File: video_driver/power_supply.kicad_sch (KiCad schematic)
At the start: 14 parts, among them J1 USB_C_Receptacle_USB2.0_16P, J2 5.5OD_2.1ID, U3 ADP2105ACPZ-3.3-R7, U4 TPS7A20xxxDBV, U5 TPS7A20xxxDBV

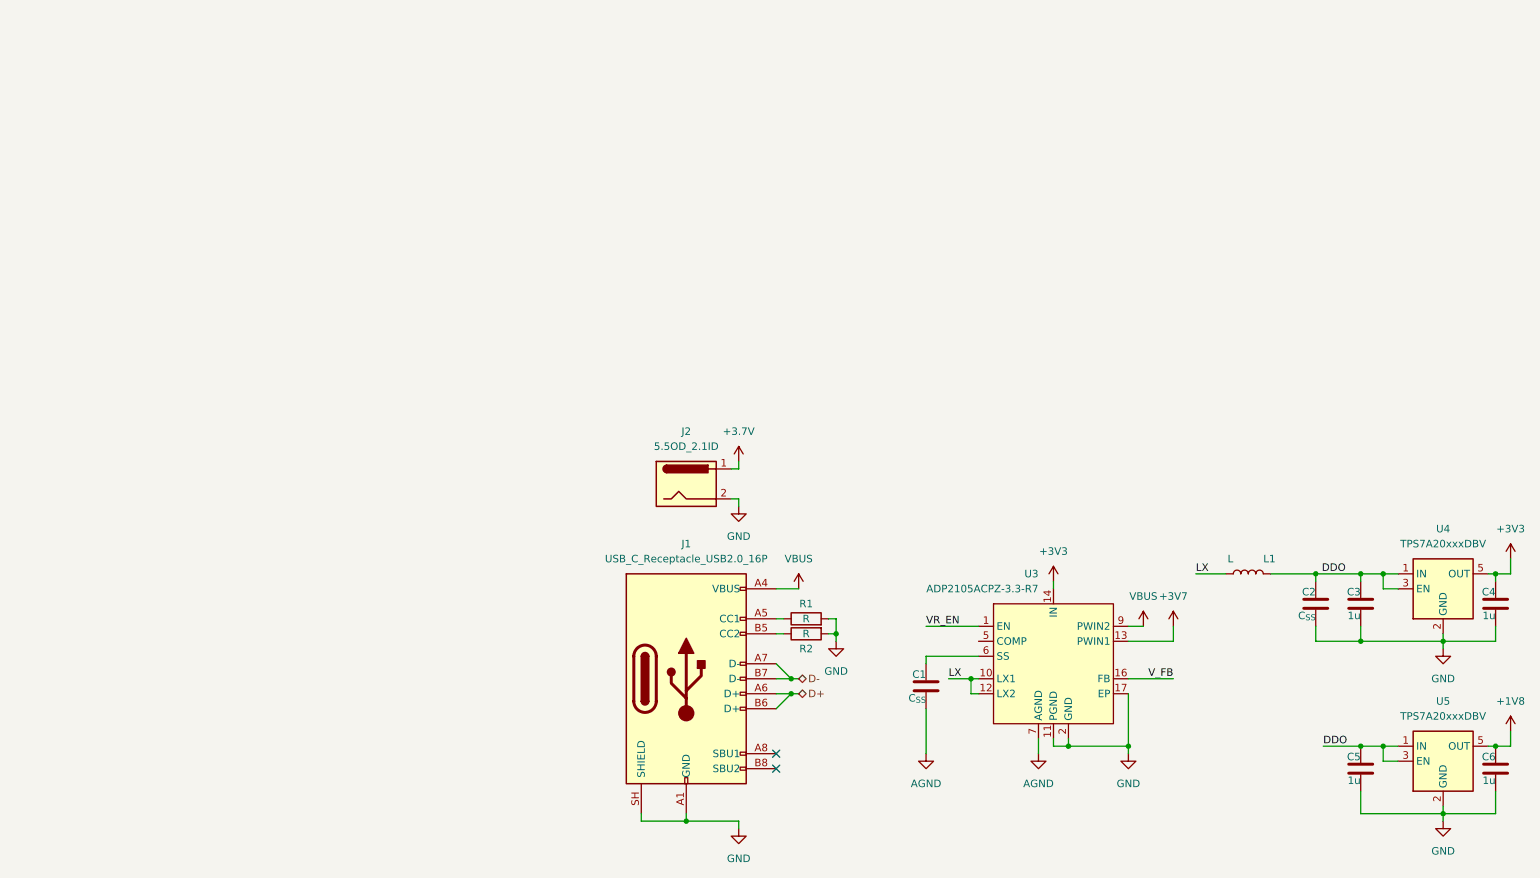
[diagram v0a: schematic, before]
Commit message: power supply start
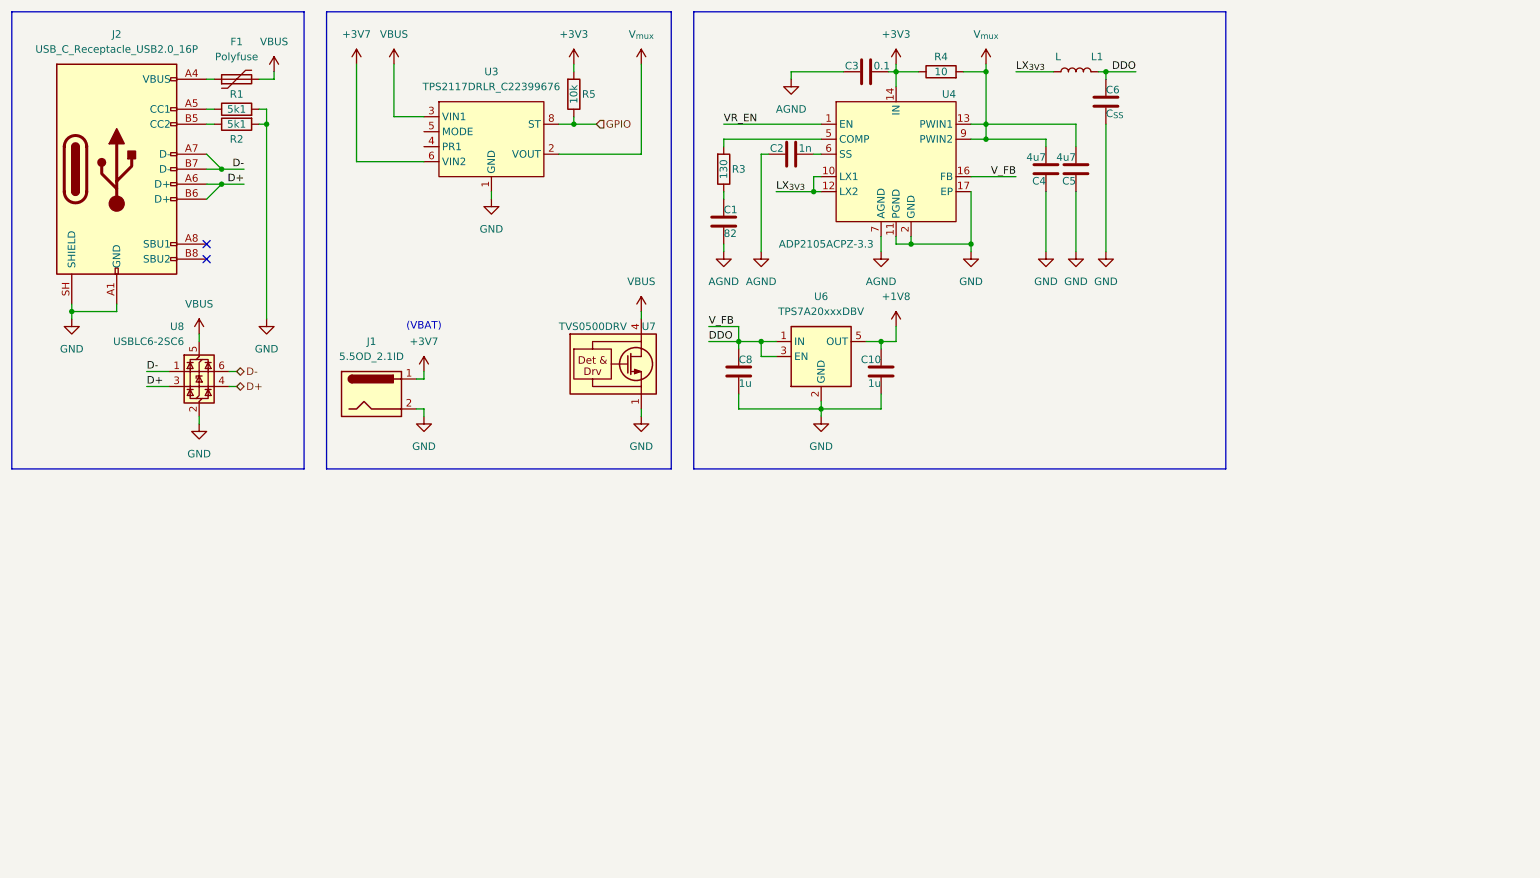
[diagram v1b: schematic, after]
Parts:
- removed U4: TPS7A20xxxDBV, Package_TO_SOT_SMD:SOT-23-5, symbol Regulator_Linear:TPS7A20xxxDBV
- added C1: 82, symbol Device:C
- added C5: 4u7, symbol Device:C
- added F1: Polyfuse, symbol Device:Polyfuse
- added R3: 130, symbol Device:R
- added R4: 10, symbol Device:R
- added R5: 10k, symbol Device:R
- added U3: TPS2117DRLR_C22399676, EasyEDA:SOT-583-8_L2.1-W1.2-P0.50-LS1.6-BL, symbol EasyEDA:TPS2117DRLR_C22399676
- added U7: TVS0500DRV, Package_SON:WSON-6-1EP_2x2mm_P0.65mm_EP1x1.6mm, symbol Power_Protection:TVS0500DRV
- added U8: USBLC6-2SC6, Package_TO_SOT_SMD:SOT-23-6, symbol Power_Protection:USBLC6-2SC6
- C2: renamed from C1; value C_{SS} -> 1n
- C3: value 1u -> 0.1
- C4: value 1u -> 4u7
- R1, R2: value R -> 5k1
- U4: renamed from U3; value ADP2105ACPZ-3.3-R7 -> ADP2105ACPZ-3.3
- renumbered C6 to C10, C2 to C6, C5 to C8, J2 to J1, J1 to J2, U5 to U6
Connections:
- net +3.7V is gone; now on net +3V7: J1.1
- net V_FB is gone; now on net DDO: U4.16 (FB)
- net +3V3: now also C3.2, R4.1, R5.2; no longer C4.1
- net +3V7: now also U3.6 (VIN2); no longer U4.13 (PWIN1)
- net AGND: now also C2.1, C3.1, C1.2; no longer C2.2
- net D+: now also U8.3 (I/O2), U8.4 (I/O2)
- net D-: now also U8.1 (I/O1), U8.6 (I/O1)
- net DDO: no longer C3.1
- net GND: now also C4.1, C5.1, U3.1 (GND), U7.1 (GND), U7.2 (GND), U7.3 (GND), U7.7 (GND), U8.2 (GND); no longer C3.2, C4.2
- net VBUS: now also F1.2, U3.3 (VIN1), U7.4 (IN), U7.5 (IN), U7.6 (IN), U8.5 (VBUS); no longer J2.A4 (VBUS), J2.A9 (VBUS), J2.B4 (VBUS), J2.B9 (VBUS), U4.9 (PWIN2)
- net at U4.5 (COMP): now also R3.2
- net at U4.6 (SS): now also C2.2; no longer C2.1
- net LX renamed LX_{3V3}
- new net: C1.1, R3.1
- new net: F1.1, J2.A4 (VBUS), J2.A9 (VBUS), J2.B4 (VBUS), J2.B9 (VBUS)
- new net GPIO: R5.1, U3.8 (ST)
- new net V_{mux}: C4.2, C5.2, R4.2, U3.2 (VOUT), U3.7 (VOUT), U4.13 (PWIN1), U4.9 (PWIN2)
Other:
- note added: "(VBAT)"
- moved on the sheet: C10, C2, C6, C8, J1, J2, L1, R1, R2, U4, U6

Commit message: power supply work
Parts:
- added C15, C16, C17, C18: 1u, symbol Device:C
- added C9: 4u7, symbol Device:C
- added F2: Polyfuse, symbol Device:Polyfuse
- added R3, R4: 5k1, symbol Device:R
- added U8, U9: TPS7A20xxxDBV, Package_TO_SOT_SMD:SOT-23-5, symbol Regulator_Linear:TPS7A20xxxDBV
- C8: renamed from C6; value C_{SS} -> 10u
- L1: value L -> 4u1
- U4: renamed from U3; value TPS2117DRLR_C22399676 -> TPS2117DRLR
- renumbered C8 to C2, C2 to C3, C3 to C4, C10 to C5, C4 to C6, C5 to C7, J2 to J1, J1 to J2, R3 to R6, R4 to R7, U8 to U3, U7 to U5, U4 to U7
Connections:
- net DDO: now also C15.1, C17.1, C9.1, U8.1 (IN), U8.3 (EN), U9.1 (IN), U9.3 (EN)
- net GND: now also C6.2, C7.2, C15.2, C16.2, C17.2, C18.2, C9.2, R4.1, U8.2 (GND), U9.2 (GND); no longer C6.1, C7.1
- net VBUS: now also U4.5 (MODE), R3.2
- net V_{mux}: now also C6.1, C7.1; no longer C6.2, C7.2
- net T_{switch}: now reaches U4.4 (PR1)
- net T_{switch}: now also R3.1, R4.2
- net +1V8 renamed +1V8_{P}
- net +3V7: no longer names the net of J2.1
- net +3V7: now also F2.2; no longer U4.6 (VIN2)
- new net +1V8_{A}: C16.1, U8.5 (OUT)
- new net +1V8_{D}: C18.1, U9.5 (OUT)
- new net VBAT: F2.1, U4.6 (VIN2)
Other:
- note added: "(+3V7)"
- note added: "V_{mux} OUT"
- note removed: "(VBAT)"
- moved on the sheet: C8, U3

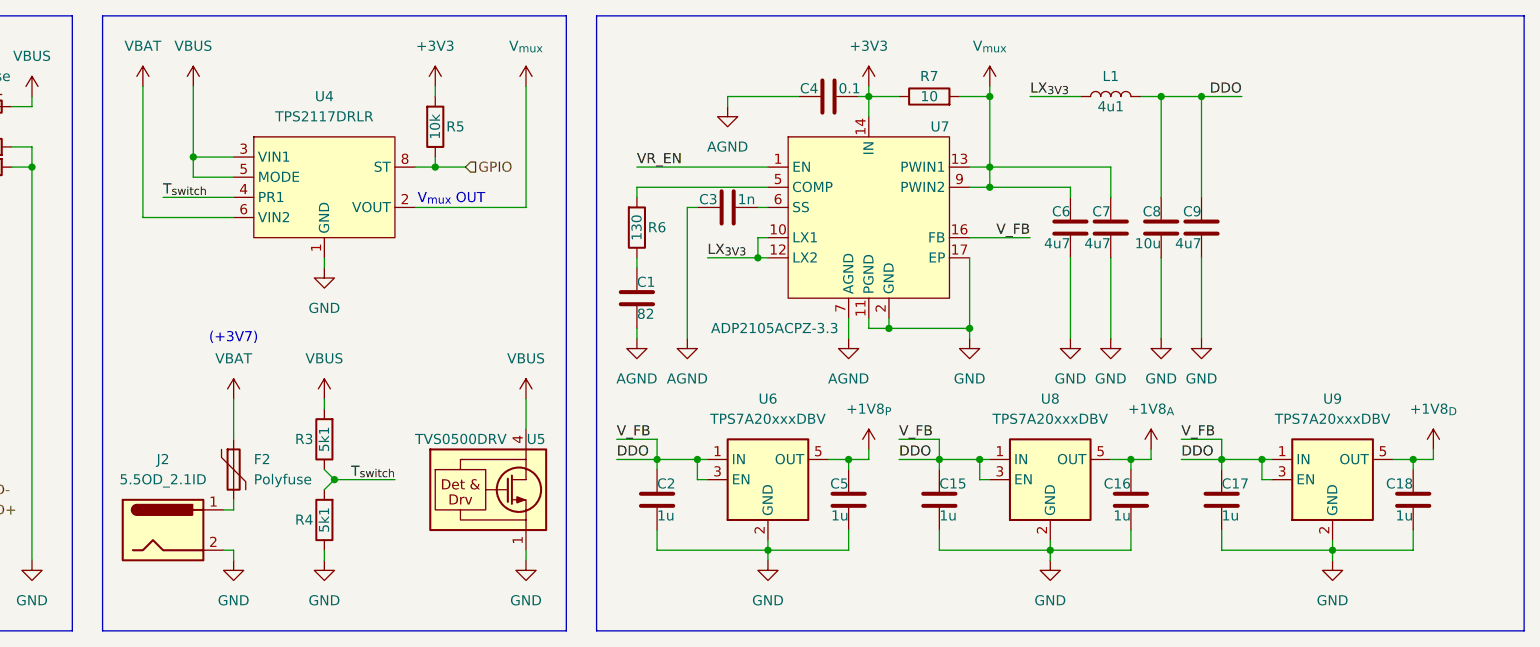
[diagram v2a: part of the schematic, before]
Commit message: new mcu
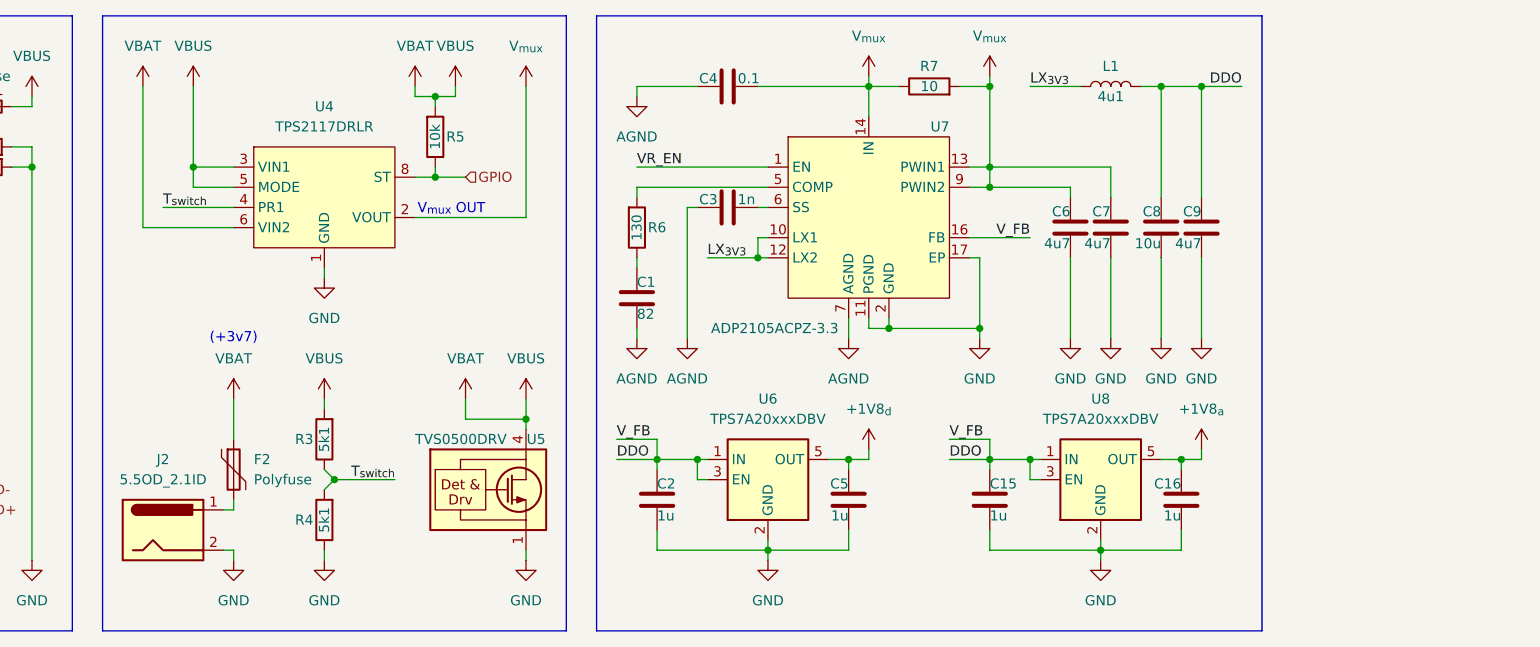
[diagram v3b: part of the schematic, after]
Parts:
- removed C17, C18: 1u, symbol Device:C
- removed U9: TPS7A20xxxDBV, Package_TO_SOT_SMD:SOT-23-5, symbol Regulator_Linear:TPS7A20xxxDBV
- C1, C15, C16, C2, C3, C4, C5, C6, C7, C8, C9: footprint (none) -> Capacitor_SMD:C_0603_1608Metric
- R1, R2, R3, R4, R5, R6, R7: footprint (none) -> Resistor_SMD:R_0402_1005Metric
- U4: footprint EasyEDA:SOT-583-8_L2.1-W1.2-P0.50-LS1.6-BL -> Package_TO_SOT_SMD:SOT-583-8
- U7: footprint EasyEDA:LFCSP-16_L4.0-W4.0-P0.65-TL-EP2.4 -> Package_CSP:Analog_LFCSP-16-1EP_4x4mm_P0.65mm_EP2.35x2.35mm
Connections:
- net VBUS is gone; now on net VBAT: F1.2, R3.2, U3.5 (VBUS), U4.3 (VIN1), U4.5 (MODE), U5.4 (IN), U5.5 (IN), U5.6 (IN)
- net VBAT: now also R5.2
- net V_{mux}: now also C4.2, R7.1, U7.14 (IN)
- net +1V8_{A} renamed +1V8_{a}
- net +1V8_{P} renamed +1V8_{d}
- removed net +3V3: C4.2, R5.2, R7.1, U7.14 (IN)
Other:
- note added: "(+3v7)"
- note removed: "(+3V7)"
- moved on the sheet: C15, C16, C4, L1, R5, R7, U4, U8
